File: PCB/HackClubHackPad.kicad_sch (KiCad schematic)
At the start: 7 parts, among them J1 Conn_01x04, SW1 SW_Push, SW2 SW_Push, SW3 SW_Push, SW4 RotaryEncoder_Switch, SW5 RotaryEncoder_Switch, U1 Seeed Studio XIAO SAMD21

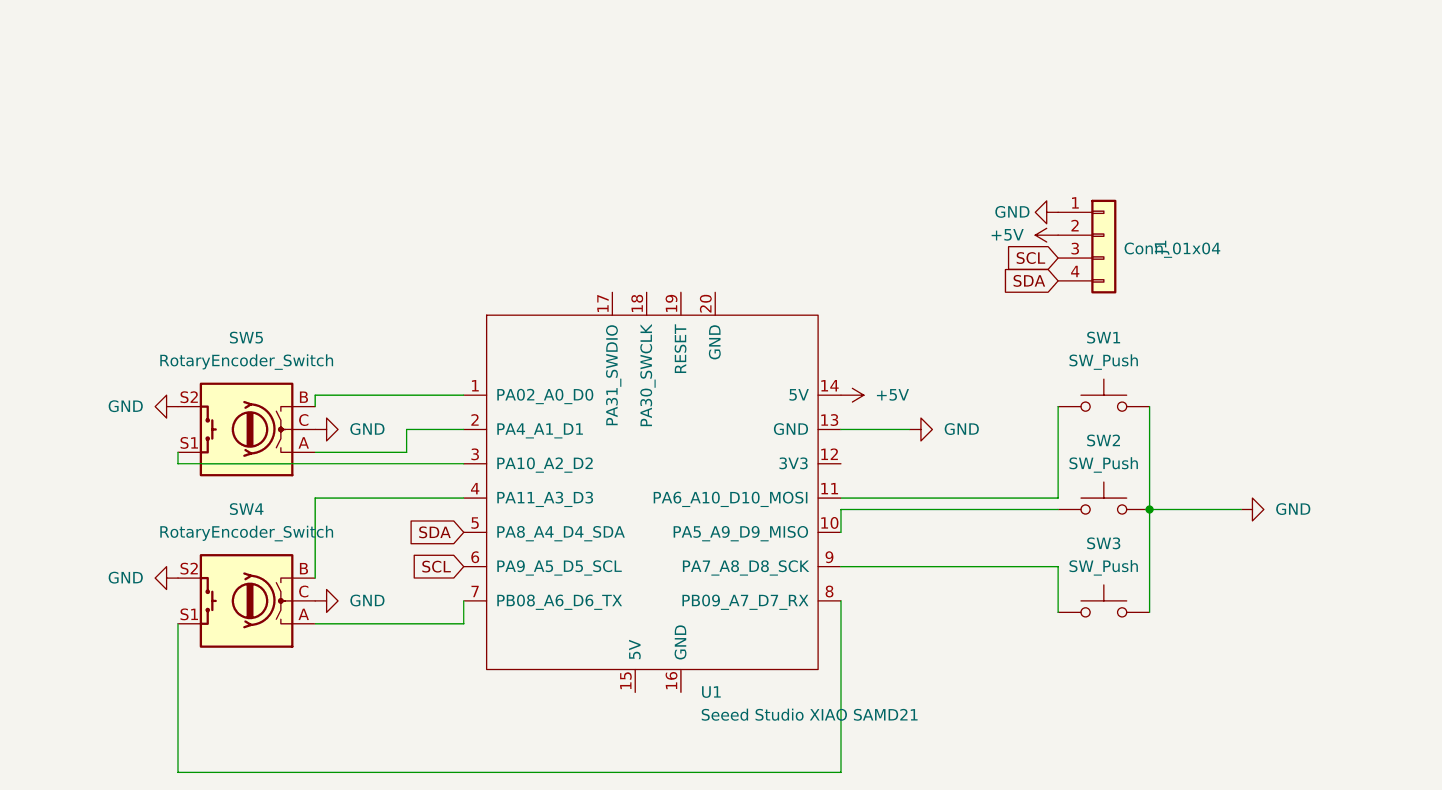
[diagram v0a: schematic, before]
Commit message: fixed firmware and changed pcb a bit
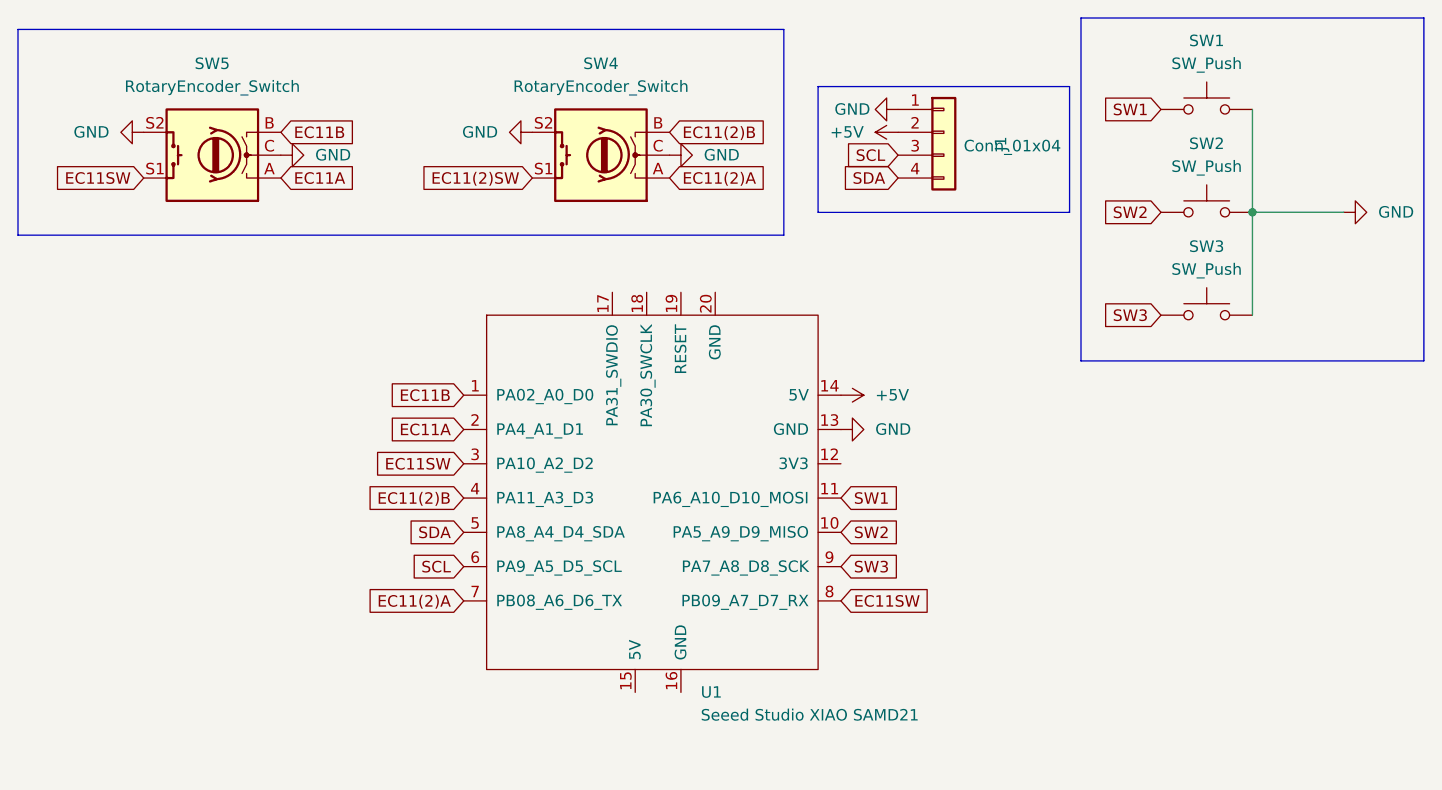
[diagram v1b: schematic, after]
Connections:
- net EC11(2)A: now reaches SW4.A, U1.7 (PB08_A6_D6_TX)
- net EC11(2)B: now reaches SW4.B, U1.4 (PA11_A3_D3)
- net EC11(2)SW: now reaches SW4.S1
- net EC11(2)SW: no longer U1.8 (PB09_A7_D7_RX)
- net SW3: now reaches SW3.1, U1.9 (PA7_A8_D8_SCK)
- net EC11A: now reaches SW5.A, U1.2 (PA4_A1_D1)
- net EC11B: now reaches SW5.B, U1.1 (PA02_A0_D0)
- net EC11SW: now reaches SW5.S1, U1.3 (PA10_A2_D2)
- net EC11SW: now also U1.8 (PB09_A7_D7_RX)
- net SW2: now reaches SW2.1, U1.10 (PA5_A9_D9_MISO)
- net SW1: now reaches SW1.1, U1.11 (PA6_A10_D10_MOSI)
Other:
- moved on the sheet: J1, SW1, SW2, SW3, SW4, SW5
